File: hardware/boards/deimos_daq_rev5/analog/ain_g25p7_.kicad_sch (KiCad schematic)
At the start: 6 parts, among them IC38001 INA826AIDR

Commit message: restore rev5 and make this rev rev6
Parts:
- removed C33006, C33007: 0.1uF, Capacitor_SMD:C_0402_1005Metric, symbol Device:C_Small
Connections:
- net +1V024 is gone; now on net GND: IC38001.6 (REF)
- net -12V is gone; now on net GND: IC38001.5 (-VS)
- net +12V renamed +3V3
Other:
- moved on the sheet: C38001

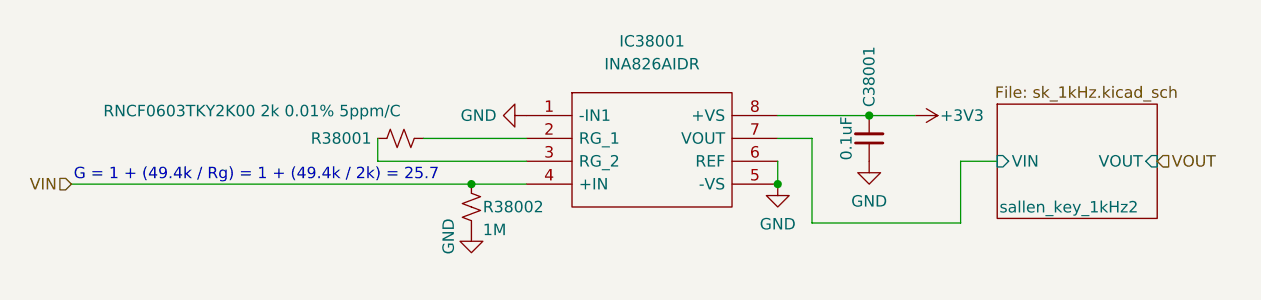
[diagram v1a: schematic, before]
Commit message: put +/12V on all inamps. add 3.3V zener behind first resistor of each filter.
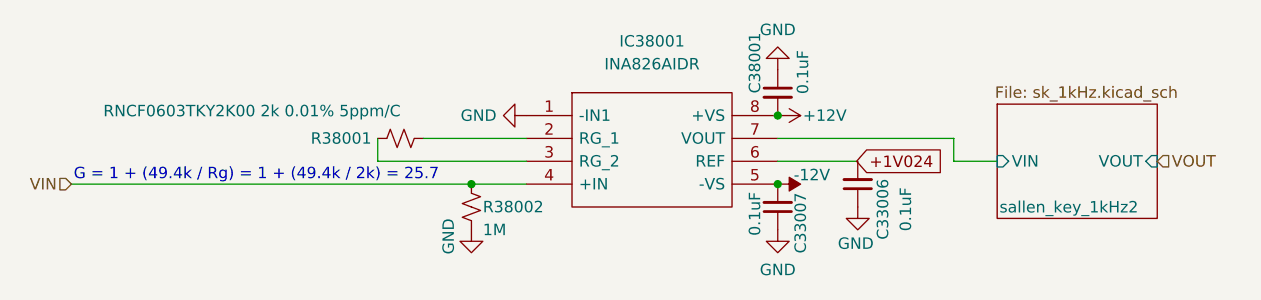
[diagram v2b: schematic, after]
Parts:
- added C33006, C33007: 0.1uF, Capacitor_SMD:C_0402_1005Metric, symbol Device:C_Small
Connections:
- net GND: now also C33006.1, C33007.1; no longer IC38001.5 (-VS), IC38001.6 (REF)
- net +3V3 renamed +12V
- new net +1V024: C33006.2, IC38001.6 (REF)
- new net -12V: C33007.2, IC38001.5 (-VS)
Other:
- moved on the sheet: C38001
